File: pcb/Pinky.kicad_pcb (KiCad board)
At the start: 2 copper layers, 142.2 x 120.5 mm, 78 parts, among them J1 MJ-4PP-9, P1 i2c-pin, P2 i2c-pin, SW1 RESET_SW, SW10 SW_PUSH, SW11 SW_PUSH, SW12 SW_PUSH, SW13 SW_PUSH, SW14 SW_PUSH, SW15 SW_PUSH, SW16 SW_PUSH, SW17 SW_PUSH, SW18 SW_PUSH, SW19 SW_PUSH, SW2 SW_PUSH, SW20 SW_PUSH, SW21 SW_PUSH, SW22 SW_PUSH, SW23 SW_PUSH, SW24 SW_PUSH, SW25 SW_PUSH, SW26 SW_PUSH, SW27 SW_PUSH, SW28 SW_PUSH, SW29 SW_PUSH, SW3 SW_PUSH, SW30 SW_PUSH, SW31 SW_PUSH, SW32 SW_PUSH, SW33 SW_PUSH, SW4 SW_PUSH, SW5 SW_PUSH, SW6 SW_PUSH, SW7 SW_PUSH, SW8 SW_PUSH, SW9 SW_PUSH, U1 ProMicro

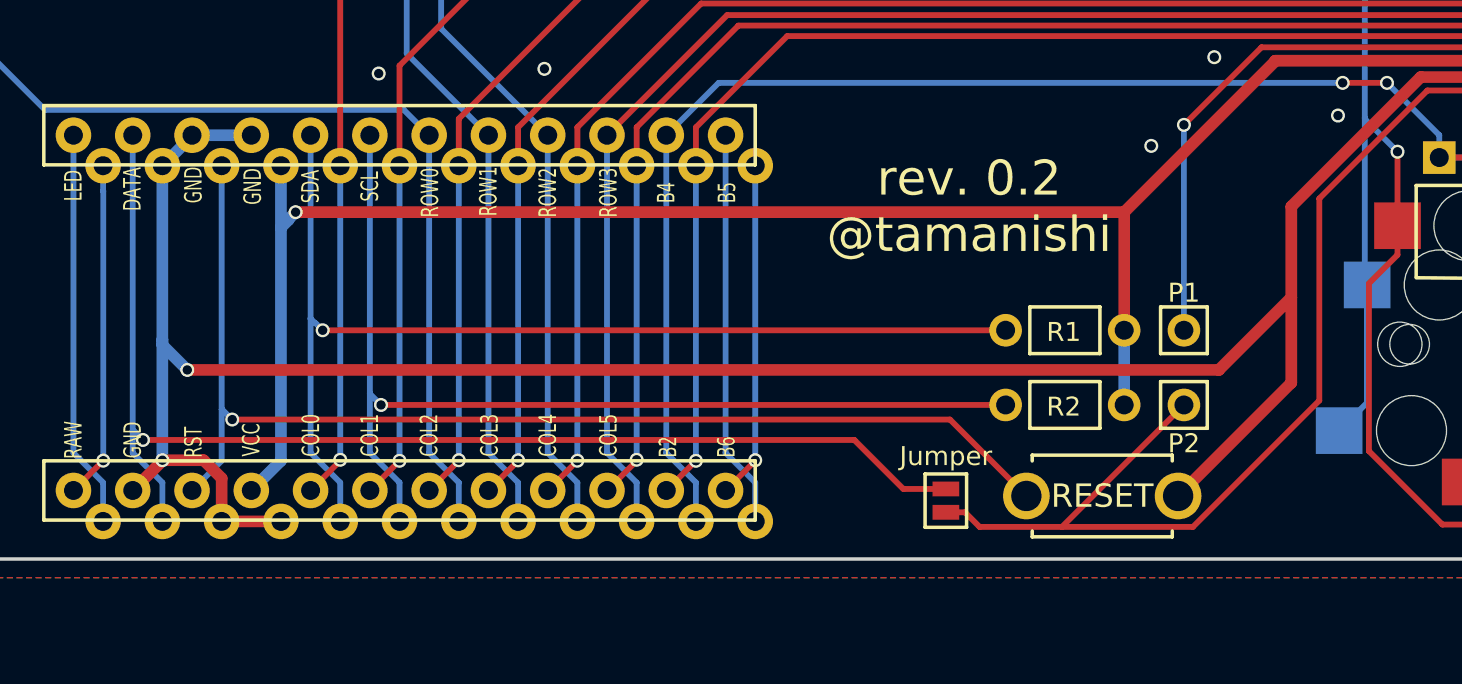
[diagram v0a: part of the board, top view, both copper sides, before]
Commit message: add HOLE_M2 for promicro cover
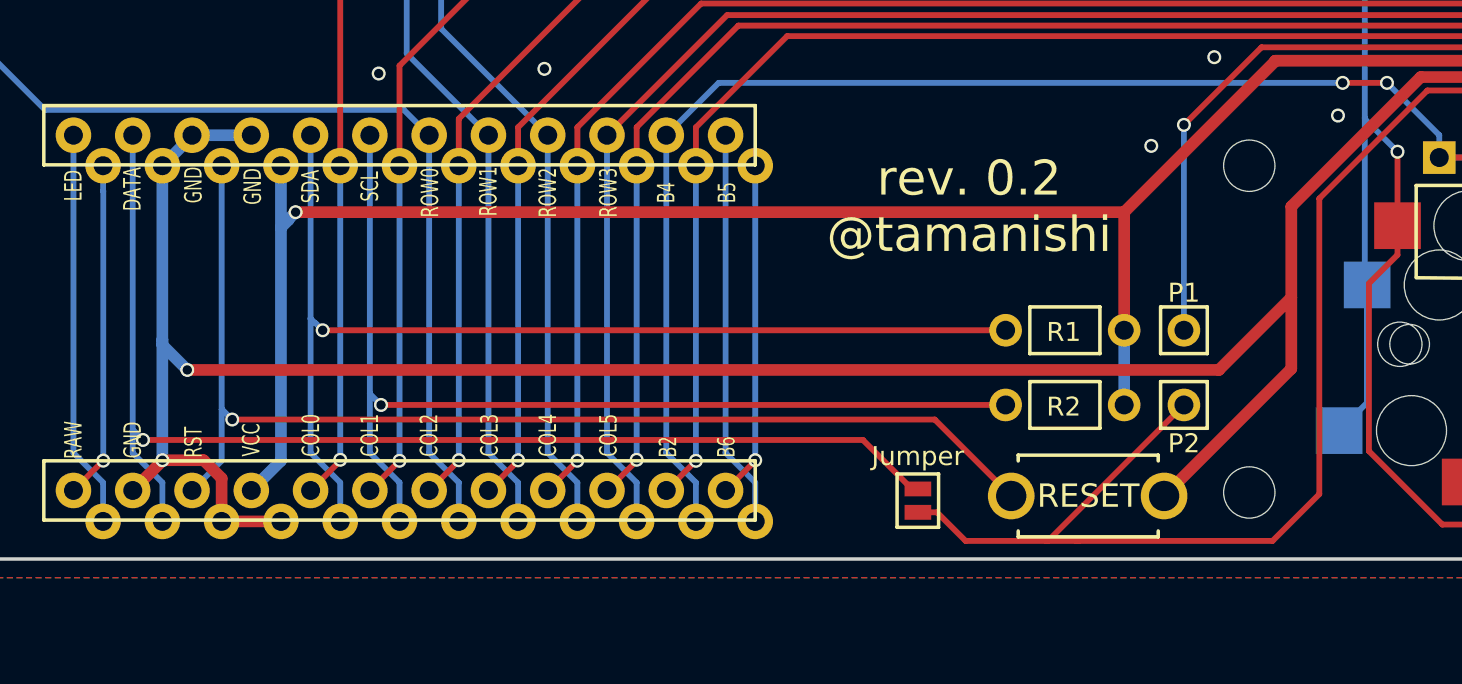
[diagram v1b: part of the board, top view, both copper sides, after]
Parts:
- added HOLE_M2: VAL**, kbd:HOLE_M2, F.Cu at (94.9, 119.4)
- added HOLE_M2: VAL**, kbd:HOLE_M2, F.Cu at (95.3, 133.9)
- moved JP1 1.20 mm to (81.0, 133.8)
- moved SW1 0.60 mm to (88.3, 133.6)
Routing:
- net Net-(J1-PadB): track 122.7 -> 127.8 mm
- net data: track 52.9 -> 51.7 mm
- net reset: track 50.5 -> 49.8 mm
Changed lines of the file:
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@@
-(kicad_pcb (version 20171130) (host pcbnew "(5.0.1-3-g963ef8bb5)")
+(kicad_pcb (version 20171130) (host pcbnew 5.0.1-33cea8e~68~ubuntu16.04.1)
   (general
     (thickness 1.6)
     (drawings 172)
-    (tracks 1108)
+    (tracks 1111)
     (zones 0)
-    (modules 78)
+    (modules 80)
     (nets 57)
   )
@@
     (mod_text_size 1 1)
     (mod_text_width 0.15)
-    (pad_size 5 5)
-    (pad_drill 4.8)
+    (pad_size 2 2)
+    (pad_drill 1.3)
     (pad_to_mask_clearance 0.2)
     (solder_mask_min_width 0.25)
@@
   )
   (module kbd:Jumper (layer F.Cu)
-    (at 82.2 133.8 90)
+    (at 81 133.8 90)
     (attr smd)
     (fp_text reference JP1 (at -2.413 0.127 90) (layer F.SilkS) hide
@@
   )
   (module kbd:ResetSW (layer F.Cu)
-    (at 88.9 133.6 180)
+    (at 88.3 133.6 180)
     (fp_text reference SW1 (at 0 2.55 180) (layer F.SilkS) hide
       (effects (font (size 1 1) (thickness 0.15)))
@@
       (effects (font (size 1 1) (thickness 0.15)))
     )
-    (pad 1 thru_hole circle (at 3.25 0 180) (size 2 2) (drill 1.3) (layers *.Cu *.Mask F.SilkS)
+    (pad 1 thru_hole circle (at 3.3 0 180) (size 2 2) (drill 1.3) (layers *.Cu *.Mask F.SilkS)
       (net 40 reset))
     (pad 2 thru_hole circle (at -3.25 0 180) (size 2 2) (drill 1.3) (layers *.Cu *.Mask F.SilkS)
@@
     )
   )
+  (module kbd:HOLE_M2 (layer F.Cu)
+    (at 94.9 119.4)
+    (fp_text reference HOLE_M2 (at 0 -2) (layer F.SilkS) hide
+      (effects (font (size 0.29972 0.29972) (thickness 0.07493)))
+    )
+    (fp_text value VAL** (at 0 1.75) (layer F.SilkS) hide
+      (effects (font (size 0.29972 0.29972) (thickness 0.0762)))
+    )
+    (pad "" np_thru_hole circle (at 0.3 0.05) (size 2.2 2.2) (drill 2.2) (layers *.Cu *.Mask F.SilkS)
+      (clearance 0.85))
+  )
+  (module kbd:HOLE_M2 (layer F.Cu)
+    (at 95.3 133.9)
+    (fp_text reference HOLE_M2 (at 0 -2) (layer F.SilkS) hide
+      (effects (font (size 0.29972 0.29972) (thickness 0.07493)))
+    )
+    (fp_text value VAL** (at 0 1.75) (layer F.SilkS) hide
+      (effects (font (size 0.29972 0.29972) (thickness 0.0762)))
+    )
+    (pad "" np_thru_hole circle (at -0.1 -0.45) (size 2.2 2.2) (drill 2.2) (layers *.Cu *.Mask F.SilkS)
+      (clearance 0.85))
+  )
   (gr_arc (start 178.313222 115.669147) (end 179.013222 115.869147) (angle -82.74675372) (layer Dwgs.User) (width 0.15))
   (gr_line (start 43 100.15) (end 43 114.15) (layer Dwgs.User) (width 0.15))
@@
   (segment (start 177.6 111.885446) (end 176.641799 112.843647) (width 0.25) (layer B.Cu) (net 37) (status 20))
   (segment (start 177.6 108.733293) (end 177.6 111.885446) (width 0.25) (layer B.Cu) (net 37))
-  (segment (start 83.0215 134.30038) (end 82.2 134.30038) (width 0.25) (layer F.Cu) (net 37) (status 20))
-  (segment (start 83.646121 134.925001) (end 83.0215 134.30038) (width 0.25) (layer F.Cu) (net 37))
-  (segment (start 87.174999 134.925001) (end 83.646121 134.925001) (width 0.25) (layer F.Cu) (net 37))
-  (segment (start 92.4 129.7) (end 87.174999 134.925001) (width 0.25) (layer F.Cu) (net 37) (status 10))
-  (segment (start 98.2 129.511002) (end 92.786001 134.925001) (width 0.25) (layer F.Cu) (net 37))
   (segment (start 102.831509 116.226489) (end 98.2 120.857998) (width 0.25) (layer F.Cu) (net 37))
   (segment (start 173.258957 116.226489) (end 102.831509 116.226489) (width 0.25) (layer F.Cu) (net 37))
-  (segment (start 92.786001 134.925001) (end 87.174999 134.925001) (width 0.25) (layer F.Cu) (net 37))
-  (segment (start 98.2 120.857998) (end 98.2 129.511002) (width 0.25) (layer F.Cu) (net 37))
   (segment (start 176.641799 112.843647) (end 173.258957 116.226489) (width 0.25) (layer F.Cu) (net 37) (status 10))
+  (segment (start 98.2 133.521002) (end 96.196001 135.525001) (width 0.25) (layer F.Cu) (net 37))
+  (segment (start 98.2 120.857998) (end 98.2 133.521002) (width 0.25) (layer F.Cu) (net 37))
+  (segment (start 81.8215 134.30038) (end 81 134.30038) (width 0.25) (layer F.Cu) (net 37) (status 20))
+  (segment (start 83.046121 135.525001) (end 81.8215 134.30038) (width 0.25) (layer F.Cu) (net 37))
+  (segment (start 87.9 135.525001) (end 87.774999 135.525001) (width 0.25) (layer F.Cu) (net 37))
+  (segment (start 96.196001 135.525001) (end 87.9 135.525001) (width 0.25) (layer F.Cu) (net 37))
+  (segment (start 86.574999 135.525001) (end 86.5 135.525001) (width 0.25) (layer F.Cu) (net 37))
+  (segment (start 92.4 129.7) (end 86.574999 135.525001) (width 0.25) (layer F.Cu) (net 37) (status 10))
+  (segment (start 86.5 135.525001) (end 83.046121 135.525001) (width 0.25) (layer F.Cu) (net 37))
+  (segment (start 87.9 135.525001) (end 86.5 135.525001) (width 0.25) (layer F.Cu) (net 37))
   (segment (start 176.205134 109.346604) (end 173.880284 111.671454) (width 0.5) (layer B.Cu) (net 38) (status 20))
   (segment (start 176.205134 106.19445) (end 176.205134 109.346604) (width 0.5) (layer B.Cu) (net 38) (status 10))
-  (segment (start 97 128.75) (end 92.15 133.6) (width 0.5) (layer F.Cu) (net 38) (status 20))
   (segment (start 52.442 118.1436) (end 49.902 118.1436) (width 0.5) (layer B.Cu) (net 38) (status 30))
   (segment (start 49.902 118.18) (end 48.632 119.45) (width 0.5) (layer B.Cu) (net 38) (status 30))
@@
   (segment (start 93.9 128.2) (end 97 125.1) (width 0.5) (layer F.Cu) (net 38))
   (segment (start 49.7 128.2) (end 93.9 128.2) (width 0.5) (layer F.Cu) (net 38))
-  (segment (start 97 125.1) (end 97 128.75) (width 0.5) (layer F.Cu) (net 38))
   (segment (start 48.632 127.132) (end 48.632 126.9) (width 0.5) (layer B.Cu) (net 38))
   (segment (start 49.7 128.2) (end 48.632 127.132) (width 0.5) (layer B.Cu) (net 38))
@@
   (via (at 160.7 126) (size 0.6) (drill 0.4) (layers F.Cu B.Cu) (net 38))
   (via (at 126.2 102.1) (size 0.6) (drill 0.4) (layers F.Cu B.Cu) (net 38))
+  (segment (start 97 125.1) (end 97 128.15) (width 0.5) (layer F.Cu) (net 38))
+  (segment (start 91.55 133.6) (end 97 128.15) (width 0.5) (layer F.Cu) (net 38) (status 10))
   (segment (start 48.632 133.024838) (end 48.632 134.69) (width 0.25) (layer B.Cu) (net 39) (status 20))
   (segment (start 47.362 131.754838) (end 48.632 133.024838) (width 0.25) (layer B.Cu) (net 39))
   (segment (start 47.362 118.1436) (end 47.362 130.8) (width 0.25) (layer B.Cu) (net 39) (status 10))
-  (segment (start 78.27812 131.2) (end 47.8 131.2) (width 0.25) (layer F.Cu) (net 39))
   (via (at 47.8 131.2) (size 0.6) (drill 0.4) (layers F.Cu B.Cu) (net 39))
   (segment (start 47.4 130.8) (end 47.362 130.8) (width 0.25) (layer B.Cu) (net 39))
   (segment (start 47.8 131.2) (end 47.4 130.8) (width 0.25) (layer B.Cu) (net 39))
   (segment (start 47.362 130.8) (end 47.362 131.754838) (width 0.25) (layer B.Cu) (net 39))
-  (segment (start 80.37774 133.29962) (end 82.2 133.29962) (width 0.25) (layer F.Cu) (net 39) (status 20))
-  (segment (start 78.27812 131.2) (end 80.37774 133.29962) (width 0.25) (layer F.Cu) (net 39))
+  (segment (start 80.746 133.29962) (end 81 133.29962) (width 0.25) (layer F.Cu) (net 39) (status 30))
+  (segment (start 78.64638 131.2) (end 80.746 133.29962) (width 0.25) (layer F.Cu) (net 39) (status 20))
+  (segment (start 47.8 131.2) (end 78.64638 131.2) (width 0.25) (layer F.Cu) (net 39))
   (segment (start 49.902 133.3636) (end 51.172 132.0936) (width 0.25) (layer B.Cu) (net 40) (status 10))
-  (segment (start 82.375001 130.325001) (end 51.625001 130.325001) (width 0.25) (layer F.Cu) (net 40))
-  (segment (start 85.65 133.6) (end 82.375001 130.325001) (width 0.25) (layer F.Cu) (net 40) (status 10))
   (via (at 51.625001 130.325001) (size 0.6) (drill 0.4) (layers F.Cu B.Cu) (net 40))
   (segment (start 51.2 129.9) (end 51.172 129.9) (width 0.25) (layer B.Cu) (net 40))
@@
   (segment (start 51.172 129.9) (end 51.172 119.45) (width 0.25) (layer B.Cu) (net 40) (status 20))
   (segment (start 51.172 132.0936) (end 51.172 129.9) (width 0.25) (layer B.Cu) (net 40))
+  (segment (start 81.725001 130.325001) (end 85 133.6) (width 0.25) (layer F.Cu) (net 40) (status 20))
+  (segment (start 51.625001 130.325001) (end 81.725001 130.325001) (width 0.25) (layer F.Cu) (net 40))
   (segment (start 56.252 119.45) (end 56.252 132.048) (width 0.25) (layer B.Cu) (net 41) (status 10))
   (via (at 56.252 132.048) (size 0.6) (drill 0.4) (layers F.Cu B.Cu) (net 41))

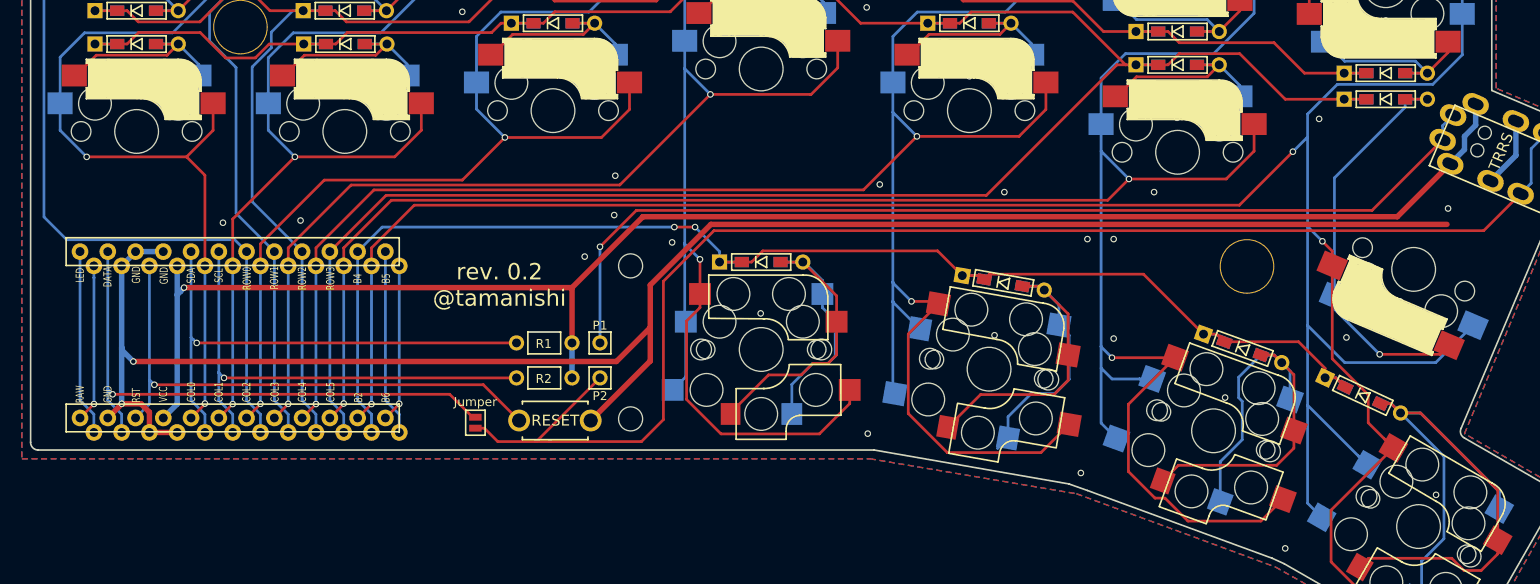
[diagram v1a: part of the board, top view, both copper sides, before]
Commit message: move promicro outside
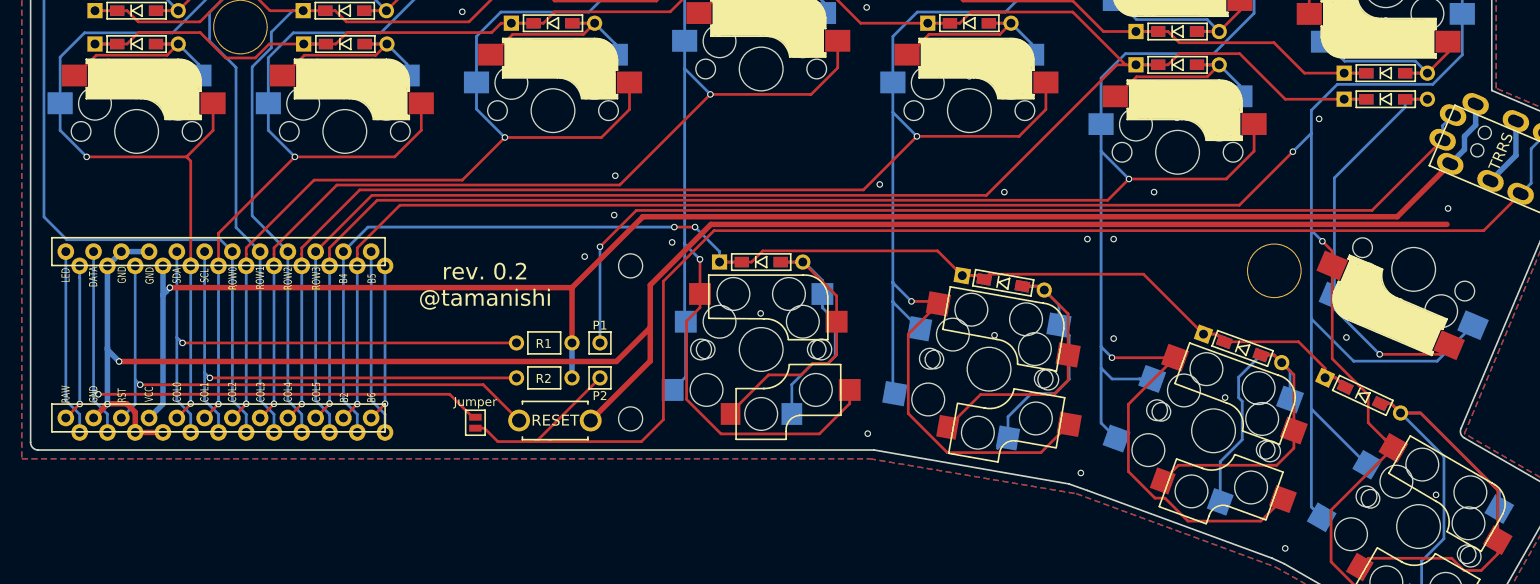
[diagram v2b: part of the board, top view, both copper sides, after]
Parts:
- moved U1 1.30 mm to (58.0, 125.8)
- moved Ref** 0.92 mm to (152.5, 119.7)
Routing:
- net row3: track 238.8 -> 240.1 mm
- net row0: track 238.1 -> 236.8 mm
- net data: track 51.7 -> 53.0 mm
- net col4: track 279.7 -> 281.0 mm
- net col3: track 266.8 -> 268.1 mm
- net reset: track 49.8 -> 51.1 mm
- net sda: track 47.1 -> 48.4 mm
- net scl: track 44.5 -> 45.8 mm
- net row4: track 125.3 -> 126.6 mm
- net VCC: track 150.7 -> 152.0 mm
- net GND: track 172.7 -> 174.0 mm, vias 58 -> 56
- net col5: track 301.2 -> 302.5 mm
- net col2: track 184.3 -> 185.4 mm
- net row2: track 185.5 -> 185.0 mm
- net row1: track 205.7 -> 205.1 mm
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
